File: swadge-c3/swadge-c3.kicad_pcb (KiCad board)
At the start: 2 copper layers, 73.7 x 89.4 mm, 67 parts, among them J1 USB_B_Micro, SW10 LEVER8184, SW11 scroll-4, SW5 4-1437565-2, SW6 4-1437565-2, SW7 4-1437565-2, SW8 4-1437565-2, SW9 SW_SPDT, U1 GS321-TR, U2 AP1117-33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

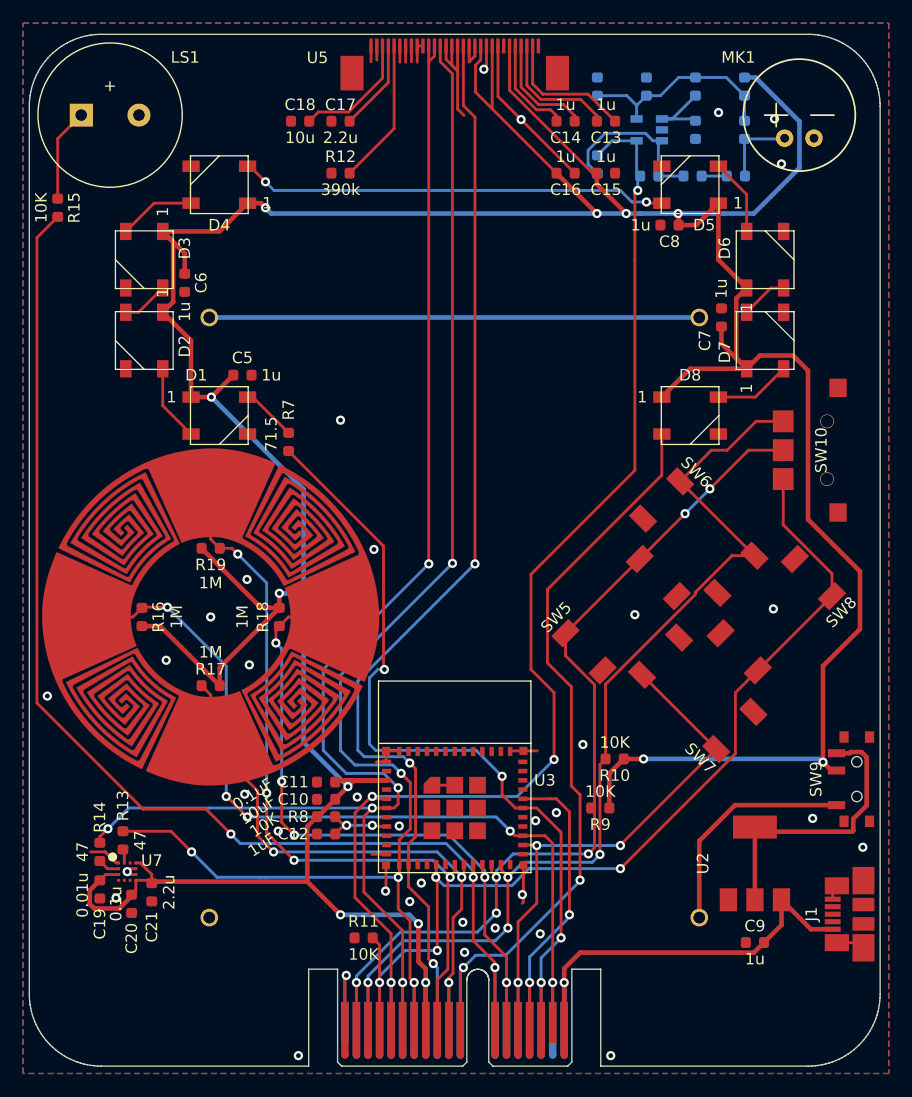
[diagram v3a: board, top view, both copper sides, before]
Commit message: Added diode, vib motor, touch ring
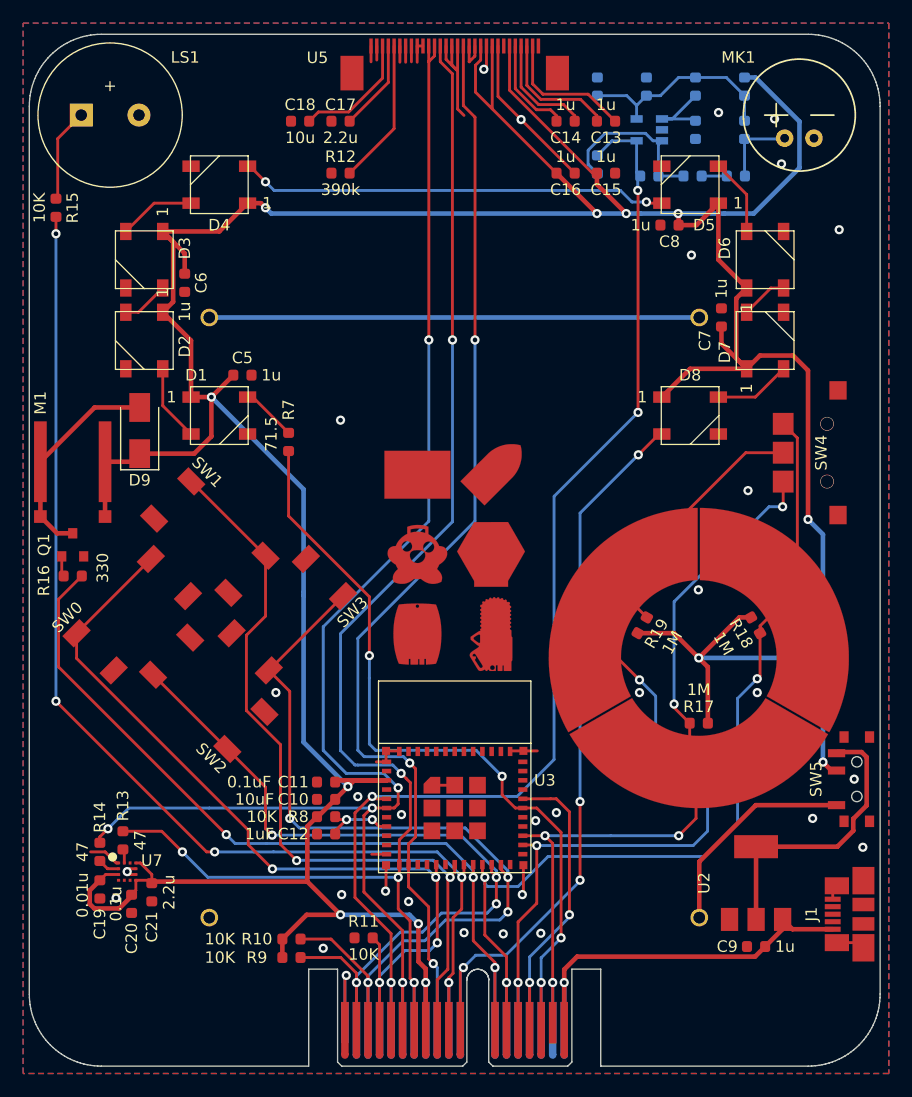
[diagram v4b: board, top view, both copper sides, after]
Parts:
- removed SW10: LEVER8184, Swadge_Parts:LEVER8184
- removed SW11: scroll-4, Swadge_Parts:scroll-4
- added D9: D, Swadge_Parts:D_SMA, F.Cu at (118.1, 92.3)
- added M1: Motor_DC, Swadge_Parts:Z30C1B839982L, F.Cu at (112.3, 91.5)
- added Q1: Q_NPN_BEC, Swadge_Parts:SOT-23, F.Cu at (112.3, 102.2)
- added Ref**: Val**, swadge-c3-art:swadges, F.Cu at (145.4, 103.3)
- added SW4: LEVER8184, Swadge_Parts:LEVER8184, F.Cu at (177.7, 94.2)
- added TC1: touch-ring-3, Swadge_Parts:touch-ring-3, F.Cu at (166.5, 112.0)
- R16: value 1M -> 330
- moved R17 42.4 mm to (166.5, 117.7)
- moved SW1 42.4 mm to (124.2, 101.5)
- moved SW2 42.4 mm to (124.1, 115.1)
- moved SW0 42.4 mm to (117.5, 108.2)
- moved SW3 42.4 mm to (130.9, 108.2)
- moved R18 41.3 mm to (171.4, 109.2), turned to 120 degrees
- moved R19 38.0 mm to (161.6, 109.2), turned to 240 degrees
- moved R10 32.1 mm to (131.2, 136.3), turned to 0 degrees
- moved R9 29.7 mm to (131.2, 137.9), turned to 0 degrees
- moved R16 6.97 mm to (112.3, 104.9), turned to 0 degrees
- moved U2 1.70 mm to (171.5, 131.5)
- moved C9 0.36 mm to (171.5, 137.0)
- moved R15 0.15 mm to (110.8, 73.0)
- renumbered SW5 to SW0, SW6 to SW1, SW7 to SW2, SW8 to SW3, SW9 to SW5
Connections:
- net IO7_SCR renamed IO7_TC0
- R10 pad 2: IO9_SW6 -> IO9_SW3
- R11 pad 2: IO10_SW8 -> IO10_SW0
- R15 pad 2: IO6_BZR -> IO5_BZR
- R16 pad 1: IO19_SCL -> Net-(Q1-Pad1)
- R16 pad 2: +3V3 -> IO6_VIB
- R17 pad 1: IO5_SCD -> IO19_TC2
- R19 pad 1: IO4_SCU -> IO18_TC1
- R9 pad 2: IO8_SW5 -> IO8_SW2
- SW0 pad 1: IO8_SW5 -> IO10_SW0
- SW0 pad 2: IO8_SW5 -> IO10_SW0
- SW1 pad 1: IO9_SW6 -> IO4_SW1
- SW1 pad 2: IO9_SW6 -> IO4_SW1
- SW2 pad 1: IO18_SW7 -> IO8_SW2
- SW2 pad 2: IO18_SW7 -> IO8_SW2
- SW3 pad 1: IO10_SW8 -> IO9_SW3
- SW3 pad 2: IO10_SW8 -> IO9_SW3
- U3 pad 16: IO10_SW8 -> IO10_SW0
- U3 pad 18: IO4_SCU -> IO4_SW1
- U3 pad 19: IO5_SCD -> IO5_BZR
- U3 pad 20: IO6_BZR -> IO6_VIB
- U3 pad 22: IO8_SW5 -> IO8_SW2
- U3 pad 23: IO9_SW6 -> IO9_SW3
- U3 pad 26: IO18_SW7 -> IO18_TC1
- U3 pad 27: IO19_SCL -> IO19_TC2
- U4 pad A10: IO5_SCD -> IO5_BZR
- U4 pad A12: IO6_BZR -> IO6_VIB
- U4 pad A14: IO18_SW7 -> IO18_TC1
- U4 pad A17: IO19_SCL -> IO19_TC2
- U4 pad A2: IO8_SW5 -> IO8_SW2
- U4 pad A3: IO9_SW6 -> IO9_SW3
- U4 pad A4: IO10_SW8 -> IO10_SW0
- U4 pad B10: IO5_SCD -> IO5_BZR
- U4 pad B12: IO6_BZR -> IO6_VIB
- U4 pad B14: IO18_SW7 -> IO18_TC1
- U4 pad B17: IO19_SCL -> IO19_TC2
- U4 pad B2: IO8_SW5 -> IO8_SW2
- U4 pad B3: IO9_SW6 -> IO9_SW3
- U4 pad B4: IO10_SW8 -> IO10_SW0
- U4 pad B9: IO4_SCU -> IO4_SW1
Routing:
- net IO6_BZR: track 107.3 -> 0.00 mm, vias 3 -> 0
- net IO5_BZR: track 0.00 -> 102.0 mm, vias 0 -> 5
- net IO9_SW6: track 89.5 -> 0.00 mm, vias 4 -> 0
- net IO18_TC1: track 0.00 -> 86.1 mm, vias 0 -> 3
- net IO10_SW8: track 85.9 -> 0.00 mm, vias 4 -> 0
- net IO8_SW5: track 82.4 -> 0.00 mm, vias 6 -> 0
- net IO9_SW3: track 0.00 -> 78.9 mm, vias 0 -> 4
- net IO10_SW0: track 0.00 -> 76.5 mm, vias 0 -> 4
- net IO19_SCL: track 75.4 -> 0.00 mm, vias 5 -> 0
- net IO6_VIB: track 0.00 -> 72.6 mm, vias 0 -> 3
- net IO8_SW2: track 0.00 -> 72.4 mm, vias 0 -> 4
- net IO19_TC2: track 0.00 -> 70.7 mm, vias 0 -> 5
- net IO4_SW1: track 0.00 -> 66.7 mm, vias 0 -> 2
- net IO4_SCU: track 64.7 -> 0.00 mm, vias 4 -> 0
- net IO5_SCD: track 52.8 -> 0.00 mm, vias 3 -> 0
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
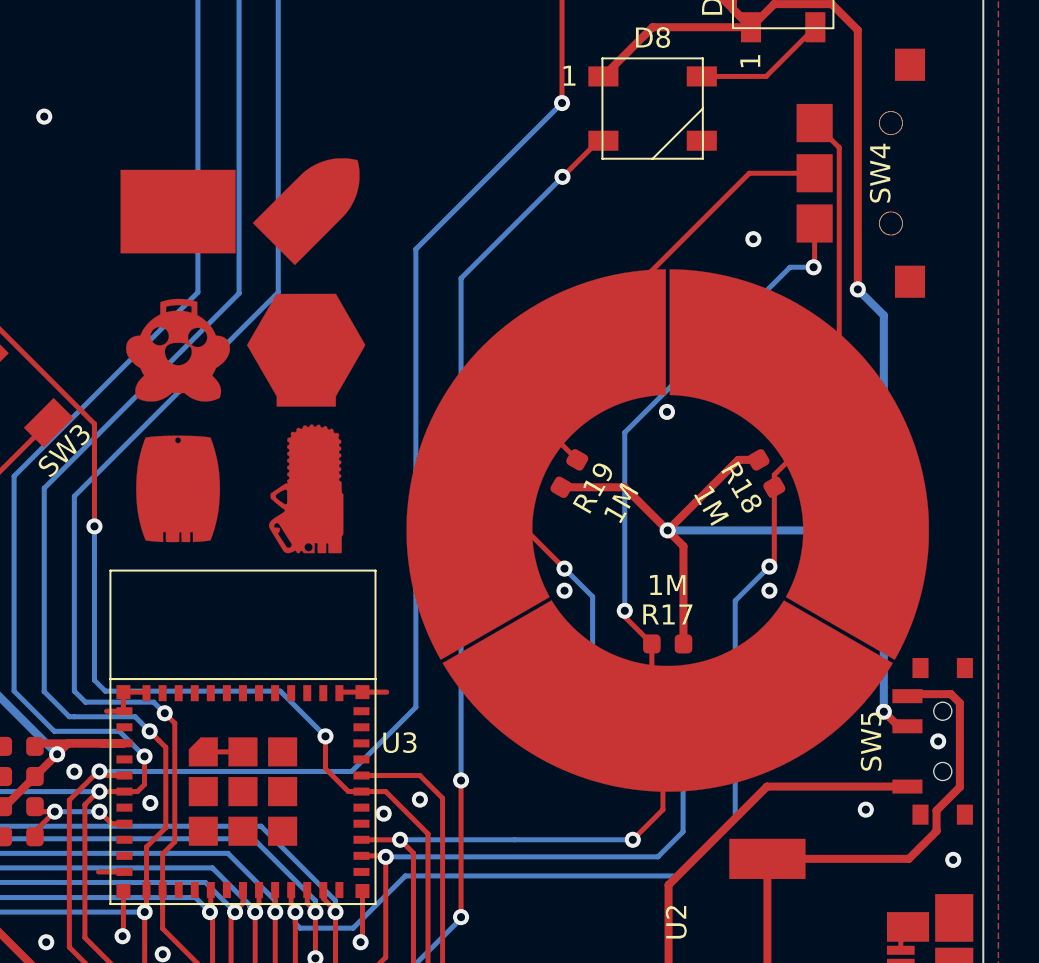
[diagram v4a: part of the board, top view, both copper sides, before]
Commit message: Fixed touch ring, added art
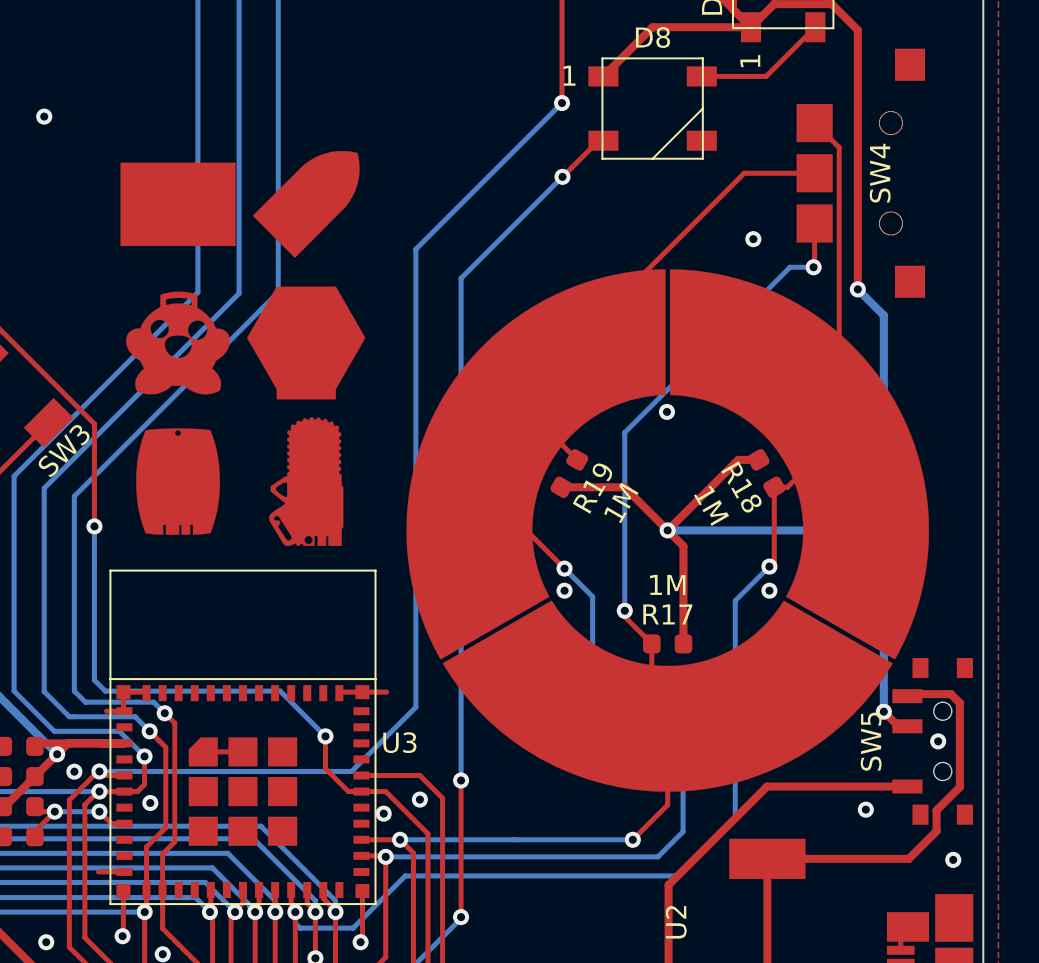
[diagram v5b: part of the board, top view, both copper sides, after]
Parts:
- moved Ref** 0.36 mm to (145.4, 102.9)
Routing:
- net IO18_TC1: track 86.1 -> 87.5 mm
- net IO7_TC0: track 81.0 -> 81.6 mm

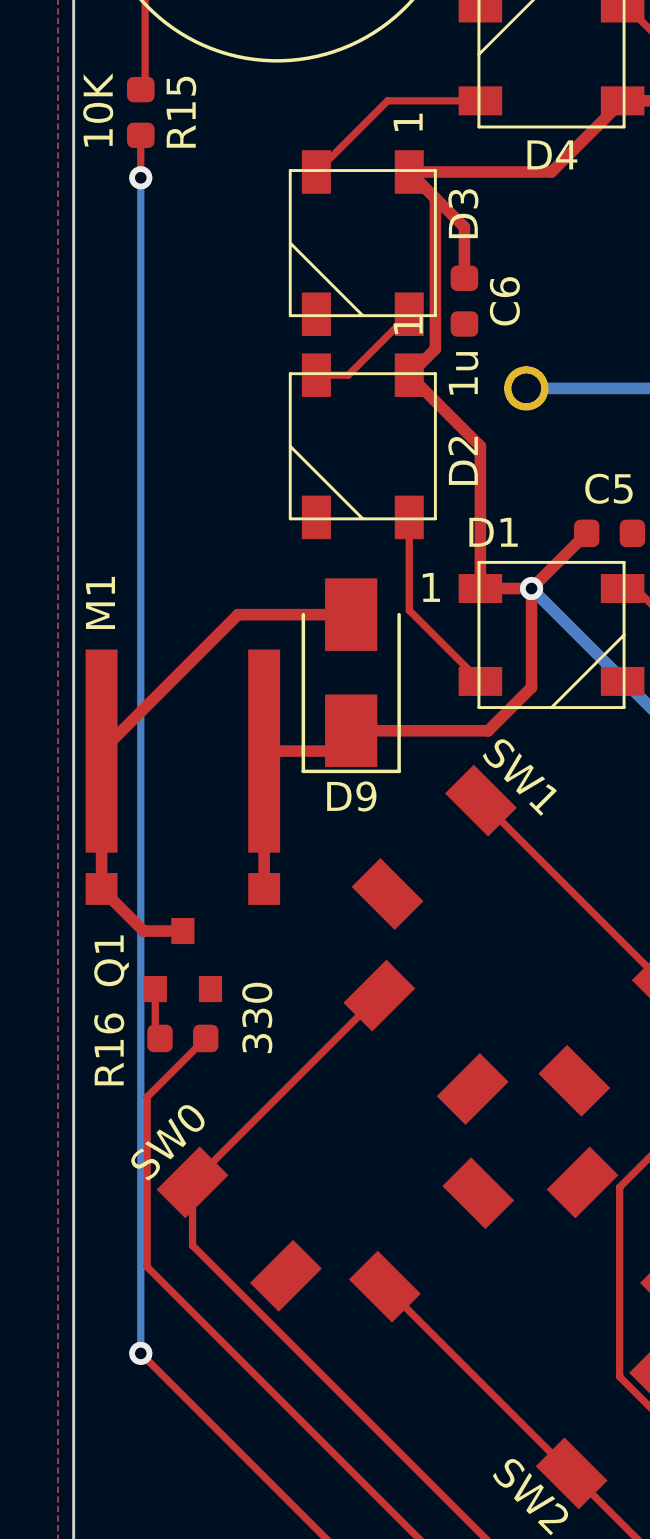
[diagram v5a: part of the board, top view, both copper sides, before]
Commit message: Update vibration motor CAD
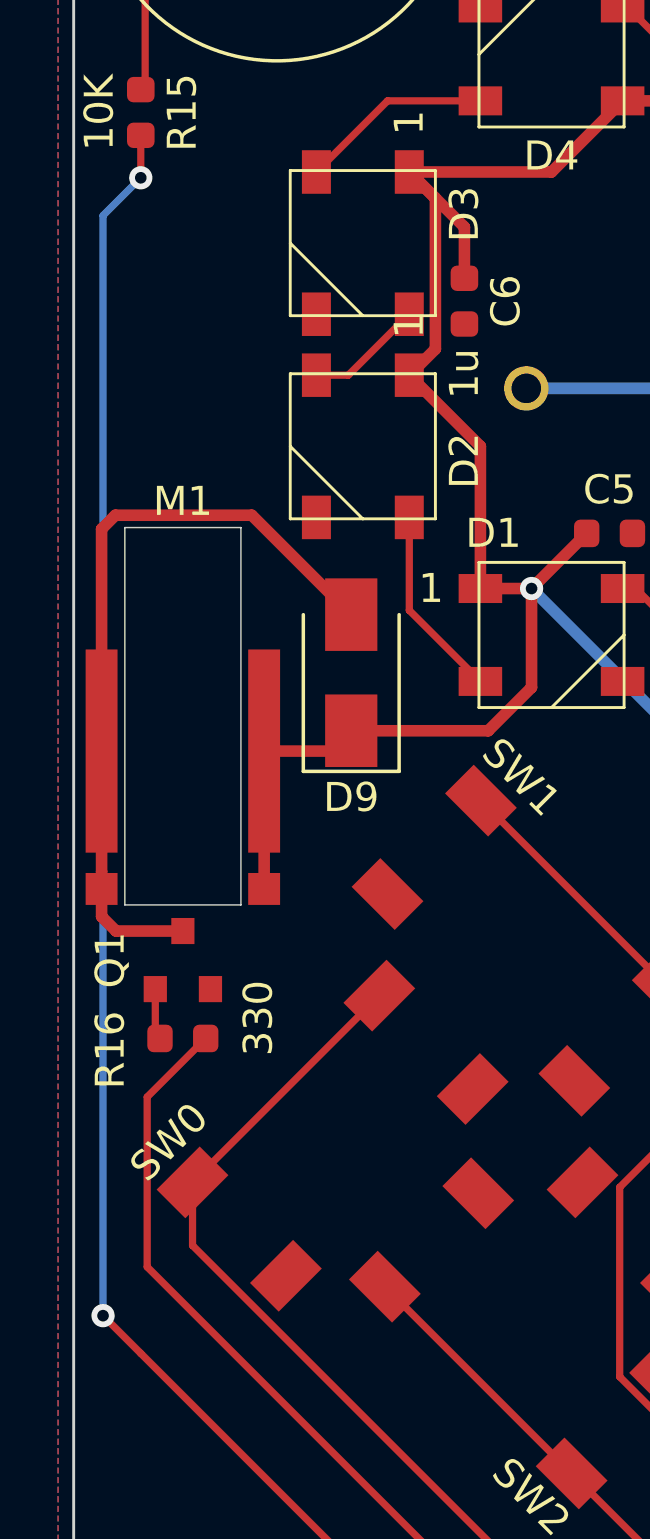
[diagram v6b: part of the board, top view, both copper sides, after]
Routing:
- net Net-(D9-Pad2): track 18.7 -> 26.6 mm
- net IO5_BZR: track 102.0 -> 103.1 mm
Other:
- outline, holes or cut-outs redrawn

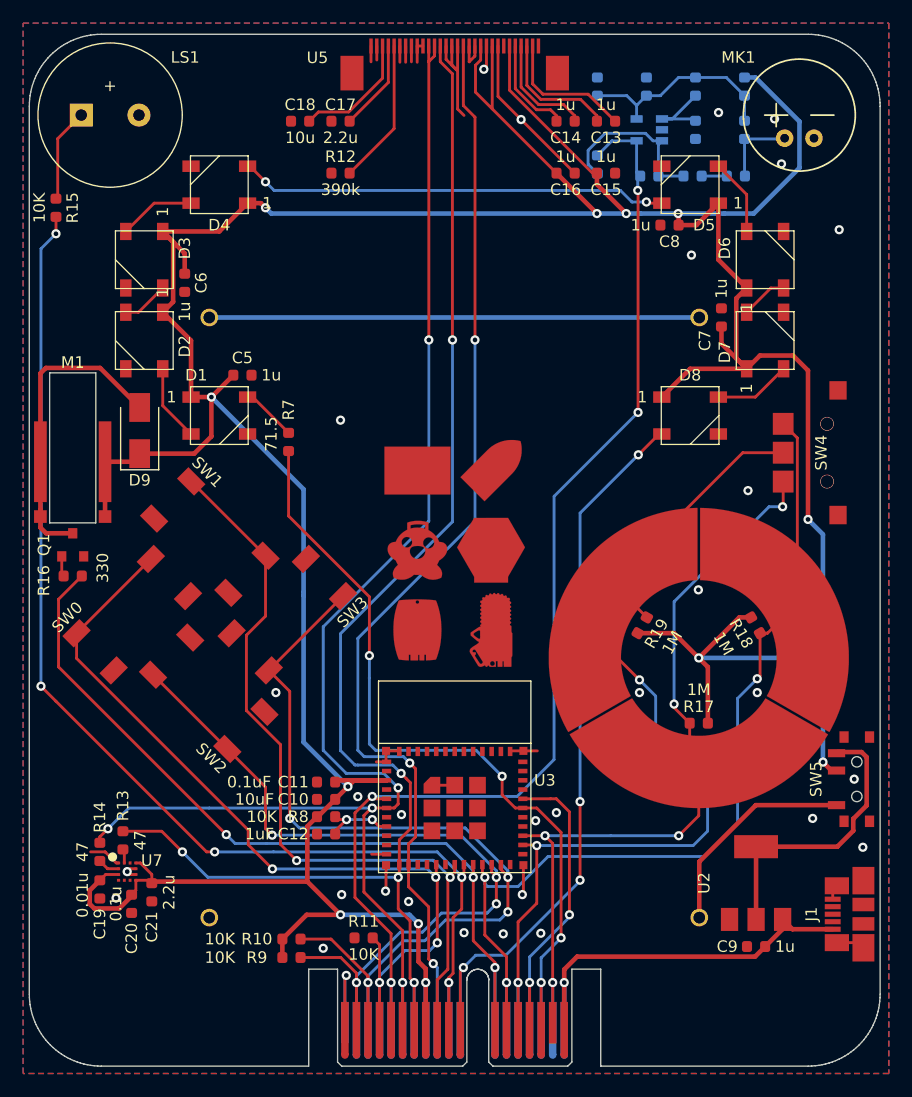
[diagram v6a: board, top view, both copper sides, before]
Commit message: Added parts for art
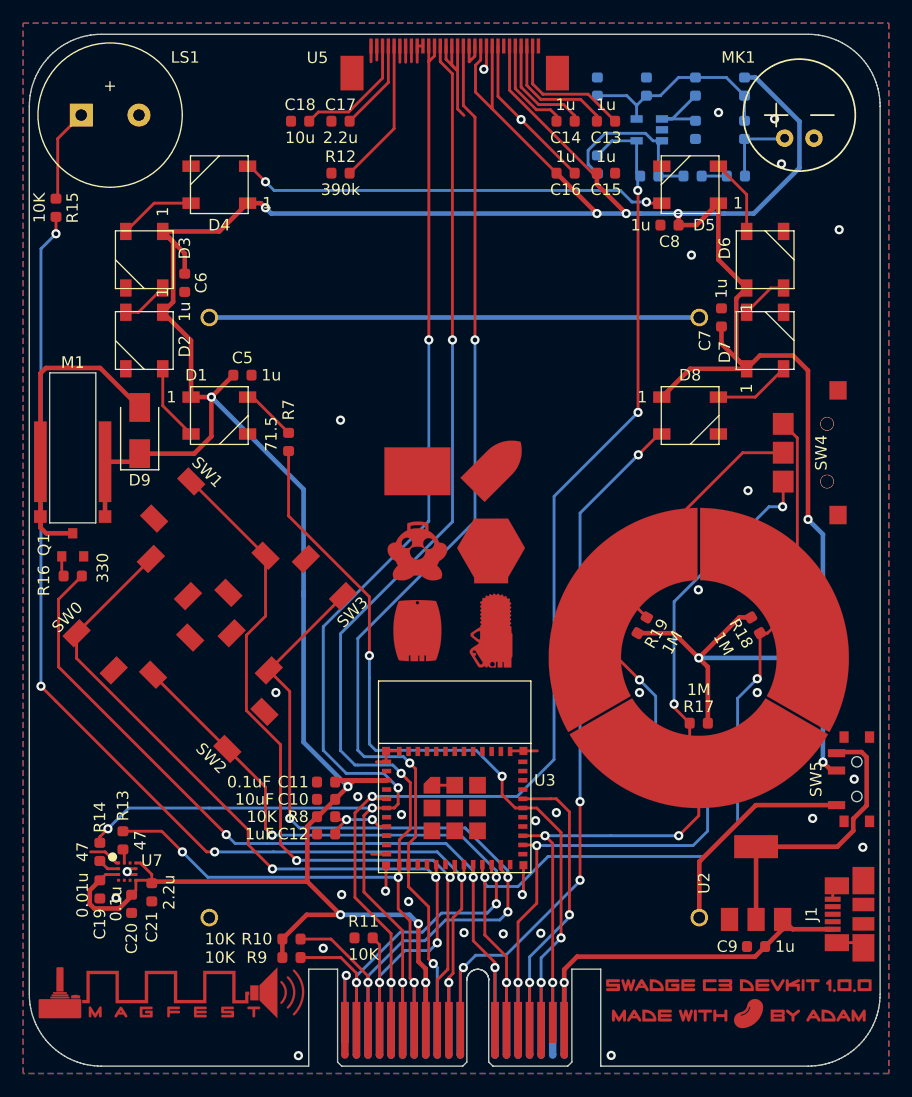
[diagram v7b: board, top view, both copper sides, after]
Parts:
- removed Ref**: Val**, swadge-c3-art:swadges
- added U10: art_swadge_family, Swadge_Parts:swadges-family, F.Cu at (145.4, 103.0)
- added U8: art_made_by_adam, Swadge_Parts:made-by-adam, F.Cu at (170.0, 141.9)
- added U9: art_mag_logo_metal, Swadge_Parts:mag-logo-metal, F.Cu at (120.8, 141.0)
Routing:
- net GND: vias 31 -> 33
